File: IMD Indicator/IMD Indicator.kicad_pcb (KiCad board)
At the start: 2 copper layers, 55.5 x 38.8 mm, 11 parts, among them J1 172448-0004, J2 172448-0004, Q1 2N7002,215

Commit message: IMD Indicator
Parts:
- moved Reset1 3.26 mm to (83.8, 55.8)
- moved D2 2.06 mm to (97.2, 61.5)
- moved R20 2.06 mm to (97.2, 56.5)
- moved D7 1.00 mm to (76.8, 58.5)
- renumbered J2 to J1, J1 to J2
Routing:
- net Net-(D5-A): track 43.3 -> 39.8 mm
- net Net-(D2-K): track 24.2 -> 21.9 mm
- net /12V IGNITION: track 57.5 -> 55.7 mm
- net IMD KILL SIGNAL: track 55.5 -> 54.0 mm
- net Net-(D7-K): track 19.1 -> 17.9 mm
- net GND: track 36.6 -> 37.6 mm
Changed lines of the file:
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@@
 		(descr "172448-YY04")
 		(tags "Connector")
-		(property "Reference" "J1"
-			(at -2.2 -2 180)
+		(property "Reference" "J2"
+			(at -2.2 -2 0)
 			(layer "F.SilkS")
 			(effects
@@
 		(descr "172448-YY04")
 		(tags "Connector")
-		(property "Reference" "J2"
+		(property "Reference" "J1"
 			(at -2.1 -2.7 180)
 			(layer "F.SilkS")
@@
 	(footprint "Resistor_SMD:R_0603_1608Metric"
 		(layer "F.Cu")
-		(at 97.675 54.5 180)
+		(at 97.175 56.5 180)
 		(descr "Resistor SMD 0603 (1608 Metric), square (rectangular) end terminal, IPC-7351 nominal, (Body size source: IPC-SM-782 page 72, https://www.pcb-3d.com/wordpress/wp-content/uploads/ipc-sm-782a_amendment_1_and_2.pdf), generated with kicad-footprint-generator")
 		(tags "resistor")
@@
 	(footprint "SDM_MiscFootprint:SOT230P700X190-4N"
 		(layer "F.Cu")
-		(at 77.85 58.5)
+		(at 76.85 58.5)
 		(descr "SOT-223")
 		(tags "SCR")
@@
 	(footprint "SDM_MiscFootprint:SODFL1608X70N"
 		(layer "F.Cu")
-		(at 97.75 59.5)
+		(at 97.25 61.5)
 		(descr "SOD-523 CASE 502")
 		(tags "Diode")
@@
 	(footprint "Button_Switch_THT:SW_PUSH_6mm"
 		(layer "F.Cu")
-		(at 87 55.5)
+		(at 83.75 55.75)
 		(descr "Generic 6mm SW tactile push button")
 		(tags "tact sw push 6mm")
@@
 	)
 	(segment
-		(start 94 79.5)
-		(end 95 80.5)
-		(width 0.2)
+		(start 96.5 61.5)
+		(end 96.5 65.5)
+		(width 0.25)
 		(layer "F.Cu")
 		(net 1)
 	)
 	(segment
-		(start 96.5 62)
-		(end 96.5 65.5)
+		(start 94 79.5)
+		(end 95 80.5)
 		(width 0.2)
 		(layer "F.Cu")
@@
 	)
 	(segment
-		(start 97 59.5)
-		(end 97 61.5)
-		(width 0.2)
-		(layer "F.Cu")
-		(net 1)
-	)
-	(segment
-		(start 97 61.5)
-		(end 96.5 62)
-		(width 0.2)
-		(layer "F.Cu")
-		(net 1)
-	)
-	(segment
 		(start 77.7 70.5)
 		(end 77.3 70.9)
@@
 	)
 	(segment
-		(start 98.5 54.5)
-		(end 98.5 59.5)
+		(start 100 64)
+		(end 98 62)
 		(width 0.5)
 		(layer "F.Cu")
@@
 	)
 	(segment
-		(start 99 75)
-		(end 98 75)
+		(start 98 61.5)
+		(end 98 56.5)
 		(width 0.5)
 		(layer "F.Cu")
@@
 	)
 	(segment
-		(start 100 64)
-		(end 100 74)
+		(start 99 75)
+		(end 98 75)
 		(width 0.5)
 		(layer "F.Cu")
@@
 	)
 	(segment
-		(start 98.5 59.5)
-		(end 98.5 62.5)
+		(start 100 64)
+		(end 100 74)
 		(width 0.5)
 		(layer "F.Cu")
@@
 	)
 	(segment
-		(start 98.5 62.5)
-		(end 100 64)
+		(start 98 62)
+		(end 98 61.5)
 		(width 0.5)
 		(layer "F.Cu")
@@
 	)
 	(segment
-		(start 74.7 60.8)
-		(end 74.7 62.8)
-		(width 0.2)
+		(start 71.5 66)
+		(end 73.7 63.8)
+		(width 0.25)
+		(layer "F.Cu")
+		(net 4)
+	)
+	(segment
+		(start 73.7 63.8)
+		(end 73.7 60.8)
+		(width 0.25)
 		(layer "F.Cu")
 		(net 4)
@@
 	)
 	(segment
-		(start 74.7 62.8)
-		(end 71.5 66)
-		(width 0.2)
-		(layer "F.Cu")
-		(net 4)
-	)
-	(segment
 		(start 74.2 79.8)
 		(end 74 80)
@@
 	)
 	(segment
-		(start 96.85 58.518)
-		(end 91.368 64)
-		(width 0.2)
-		(layer "F.Cu")
-		(net 5)
-	)
-	(segment
-		(start 91.368 64)
-		(end 91.368 65.5)
-		(width 0.2)
-		(layer "F.Cu")
-		(net 5)
-	)
-	(segment
-		(start 96.85 54.5)
-		(end 96.85 58.518)
-		(width 0.2)
-		(layer "F.Cu")
-		(net 5)
-	)
-	(segment
-		(start 90.868 66)
-		(end 88.5 66)
-		(width 0.2)
+		(start 96.35 58.15)
+		(end 96.35 56.5)
+		(width 0.25)
 		(layer "F.Cu")
 		(net 5)
 	)
 	(segment
-		(start 91.368 65.5)
-		(end 90.868 66)
-		(width 0.2)
+		(start 88.5 66)
+		(end 96.35 58.15)
+		(width 0.25)
 		(layer "F.Cu")
 		(net 5)
@@
 	)
 	(segment
-		(start 85.96 84.5)
-		(end 85.96 84.96)
-		(width 0.2)
-		(layer "F.Cu")
-		(net 6)
-	)
-	(segment
 		(start 92.5 75)
 		(end 92.5 76.96)
@@
 	)
 	(segment
-		(start 81 64.5)
-		(end 74.854 70.646)
+		(start 80 58.5)
+		(end 73.7 58.5)
 		(width 0.25)
 		(layer "F.Cu")
@@
 	)
 	(segment
-		(start 85.96 84.96)
-		(end 86 85)
-		(width 0.2)
+		(start 74.854 70.646)
+		(end 80 65.5)
+		(width 0.25)
 		(layer "F.Cu")
 		(net 6)
 	)
 	(segment
-		(start 81 58.5)
-		(end 74.7 58.5)
+		(start 74.854 70.646)
+		(end 74.854 80.536)
 		(width 0.25)
 		(layer "F.Cu")
@@
 	)
 	(segment
-		(start 81 58.5)
-		(end 81 64.5)
+		(start 74.854 80.536)
+		(end 77.818 83.5)
 		(width 0.25)
 		(layer "F.Cu")
@@
 	)
 	(segment
-		(start 74.854 70.646)
-		(end 74.854 80.536)
+		(start 80 65.5)
+		(end 80 58.5)
 		(width 0.25)
 		(layer "F.Cu")
@@
 	)
 	(segment
-		(start 85.96 85.04)
-		(end 85.96 84.5)
+		(start 73.7 56.2)
+		(end 83.3 56.2)
 		(width 0.25)
 		(layer "F.Cu")
-		(net 6)
+		(net 7)
 	)
 	(segment
-		(start 74.854 80.536)
-		(end 77.818 83.5)
+		(start 83.75 55.75)
+		(end 83.25 55.75)
 		(width 0.25)
 		(layer "F.Cu")
-		(net 6)
+		(net 7)
 	)
 	(segment
-		(start 93.5 55.5)
-		(end 87 55.5)
-		(width 0.2)
+		(start 83.3 56.2)
+		(end 83.75 55.75)
+		(width 0.25)
 		(layer "F.Cu")
 		(net 7)
 	)
 	(segment
-		(start 74.7 56.2)
-		(end 86.3 56.2)
+		(start 90.25 55.75)
+		(end 83.75 55.75)
 		(width 0.25)
 		(layer "F.Cu")
@@
 	)
 	(segment
-		(start 86.3 56.2)
-		(end 87 55.5)
+		(start 84.3 56.2)
+		(end 84.75 55.75)
 		(width 0.25)
 		(layer "F.Cu")
@@
 	)
 	(segment
-		(start 85.65 69.35)
+		(start 84.55 66.55)
 		(end 85.65 67.65)
 		(width 0.2)
@@
 	)
 	(segment
-		(start 84.5 70.5)
-		(end 85.65 69.35)
+		(start 84.55 65.05)
+		(end 84.55 66.55)
 		(width 0.2)
 		(layer "F.Cu")
@@
 	)
 	(segment
-		(start 84.5 65)
-		(end 84.55 65.05)
+		(start 85.65 69.35)
+		(end 85.65 67.65)
 		(width 0.2)
 		(layer "F.Cu")
@@
 	)
 	(segment
-		(start 85.65 67.65)
-		(end 84.5 66.5)
+		(start 84.5 70.5)
+		(end 85.65 69.35)
 		(width 0.2)
 		(layer "F.Cu")
@@
 	)
 	(segment
-		(start 84.5 66.5)
-		(end 84.5 65)
-		(width 0.2)
-		(layer "F.Cu")
-		(net 8)
-	)
-	(segment
 		(start 92.075 82)
 		(end 90.575 83.5)
@@
 	)
 	(segment
-		(start 87 60)
-		(end 87.626 60.626)
-		(width 0.2)
+		(start 87.5 65.75)
+		(end 86.3 66.95)
+		(width 0.25)
 		(layer "F.Cu")
 		(net 10)
 	)
 	(segment
-		(start 87.626 60.626)
-		(end 87.626 65.624)
+		(start 90.25 60.25)
+		(end 83.75 60.25)
 		(width 0.5)
 		(layer "F.Cu")
@@
 	)
 	(segment
-		(start 83.3 74.6)
-		(end 82.8 75.1)
-		(width 0.2)
+		(start 87.5 64)
+		(end 87.5 65.75)
+		(width 0.25)
 		(layer "F.Cu")
 		(net 10)
 	)
 	(segment
-		(start 87.626 65.624)
-		(end 86.3 66.95)
-		(width 0.5)
+		(start 83.3 74.6)
+		(end 82.8 75.1)
+		(width 0.2)
 		(layer "F.Cu")
 		(net 10)
@@
 	)
 	(segment
-		(start 85.5 71.5)
-		(end 85.5 72.4)
-		(width 0.5)
-		(layer "B.Cu")
+		(start 83.75 60.25)
+		(end 87.5 64)
+		(width 0.25)
+		(layer "F.Cu")
 		(net 10)
 	)
 	(segment
-		(start 87 60)
-		(end 93.5 60)
+		(start 85.5 71.5)
+		(end 85.5 72.4)
 		(width 0.5)
 		(layer "B.Cu")

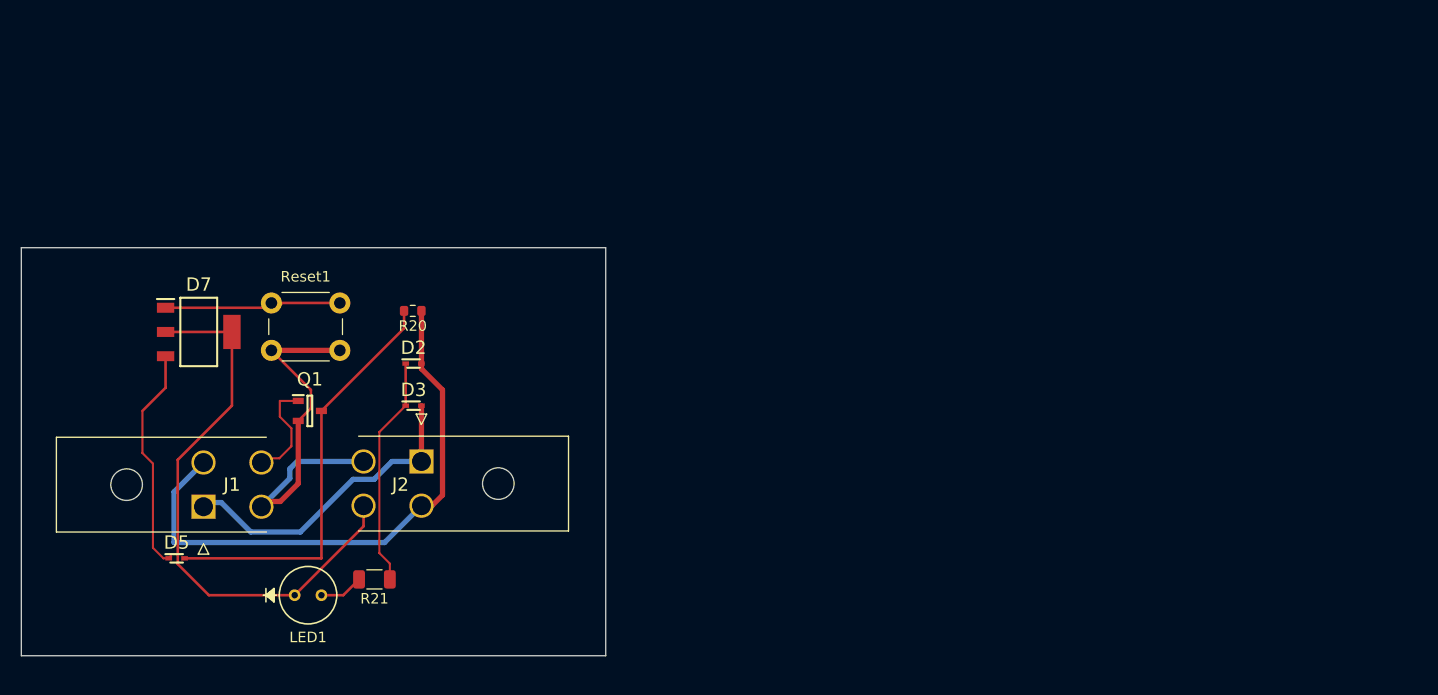
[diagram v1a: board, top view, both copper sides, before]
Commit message: fixed reset button and connect logic signal to SCR gate
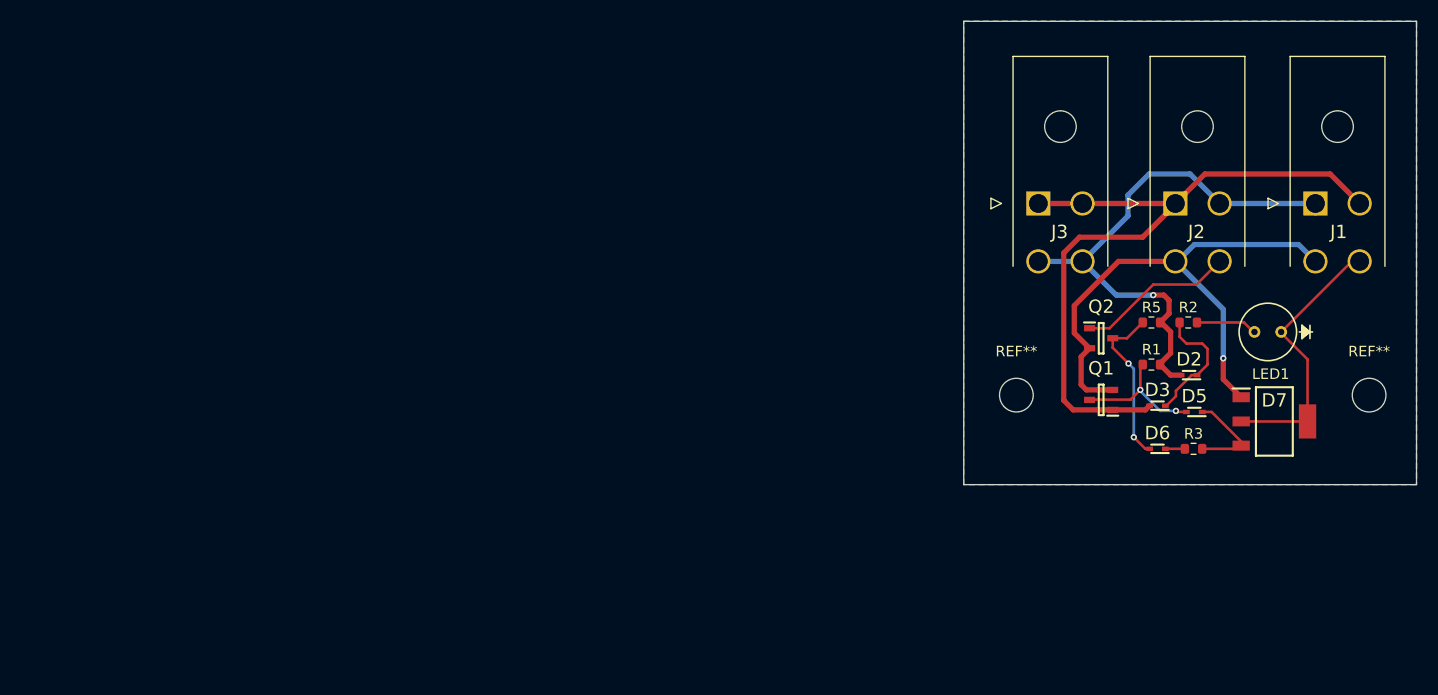
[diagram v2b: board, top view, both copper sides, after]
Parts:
- removed R20: 10k, Resistor_SMD:R_0603_1608Metric
- removed R21: 510, Resistor_SMD:R_1206_3216Metric
- removed Reset1: SW_Push_Open, Button_Switch_THT:SW_PUSH_6mm
- added D6: BAT54XV2T1G, SDM_MiscFootprint:SODFL1608X70N, F.Cu at (167.9, 69.6)
- added J3: 172448-0004, IMDFootprintLibrary:172448-YY04, F.Cu at (156.6, 46.3)
- added Q2: 2N7002,215, SDM_MiscFootprint:SOT95P230X110-3N, F.Cu at (162.6, 59.1)
- added R1: 10k, Resistor_SMD:R_0603_1608Metric, F.Cu at (167.3, 61.6)
- added R2: 510, Resistor_SMD:R_0603_1608Metric, F.Cu at (170.8, 57.6)
- added R3: 1k, Resistor_SMD:R_0603_1608Metric, F.Cu at (171.3, 69.6)
- added R5: 10k, Resistor_SMD:R_0603_1608Metric, F.Cu at (167.3, 57.6)
- added REF**: MountingHole_3.2mm_M3, MountingHole:MountingHole_3.2mm_M3, F.Cu at (154.5, 64.5)
- added REF**: MountingHole_3.2mm_M3, MountingHole:MountingHole_3.2mm_M3, F.Cu at (188.0, 64.5)
- moved J1 109.5 mm to (182.9, 46.3), turned to 180 degrees
- moved D7 102.5 mm to (179.0, 67.0)
- moved D5 97.6 mm to (171.4, 66.1), turned to 180 degrees
- moved LED1 97.0 mm to (179.7, 58.5), turned to 180 degrees
- moved J2 75.7 mm to (169.6, 46.3), turned to 180 degrees
- moved Q1 75.2 mm to (162.6, 65.0), turned to 180 degrees
- moved D2 73.7 mm to (170.9, 62.6), turned to 180 degrees
- moved D3 70.7 mm to (167.9, 65.5), turned to 180 degrees
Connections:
- D7 pad 1: Net-(D7-K) -> GND
- J1 pad 1: /12V MASTER -> /12V IGNITION
- J1 pad 2: /12V IGNITION -> /12V MASTER
- J1 pad 4: /IMD_Logic_Signal -> IMD KILL SIGNAL
- J2 pad 4: IMD KILL SIGNAL -> /IMD_LOGIC_SIGNAL
- Q1 pad 1: /IMD_Logic_Signal -> /12V MASTER
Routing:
- net /12V MASTER: track 30.1 -> 68.7 mm
- net IMD KILL SIGNAL: track 54.0 -> 25.6 mm
- net Net-(D5-A): track 39.8 -> 13.4 mm, vias 0 -> 2
- net Net-(D7-K): track 17.9 -> 0.00 mm
- net GND: track 37.6 -> 53.4 mm, vias 0 -> 1
- net Net-(D6-A): track 0.00 -> 15.7 mm, vias 0 -> 2
- net /IMD_LOGIC_SIGNAL: track 0.00 -> 15.0 mm
- net /SCR Gate: track 21.7 -> 8.85 mm
- net Net-(D2-K): track 21.9 -> 11.9 mm
- net /IMD_Logic_Signal: track 10.00 -> 0.00 mm
- net /12V IGNITION: track 55.7 -> 52.6 mm, vias 0 -> 1
- net Net-(D6-K): track 0.00 -> 1.85 mm
- net Net-(LED1-Pad2): track 4.20 -> 5.87 mm
- added copper zone on B.Cu, net GND
- added copper zone on F.Cu, net GND
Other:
- board size 55.5 x 38.8 mm -> 43 x 44 mm

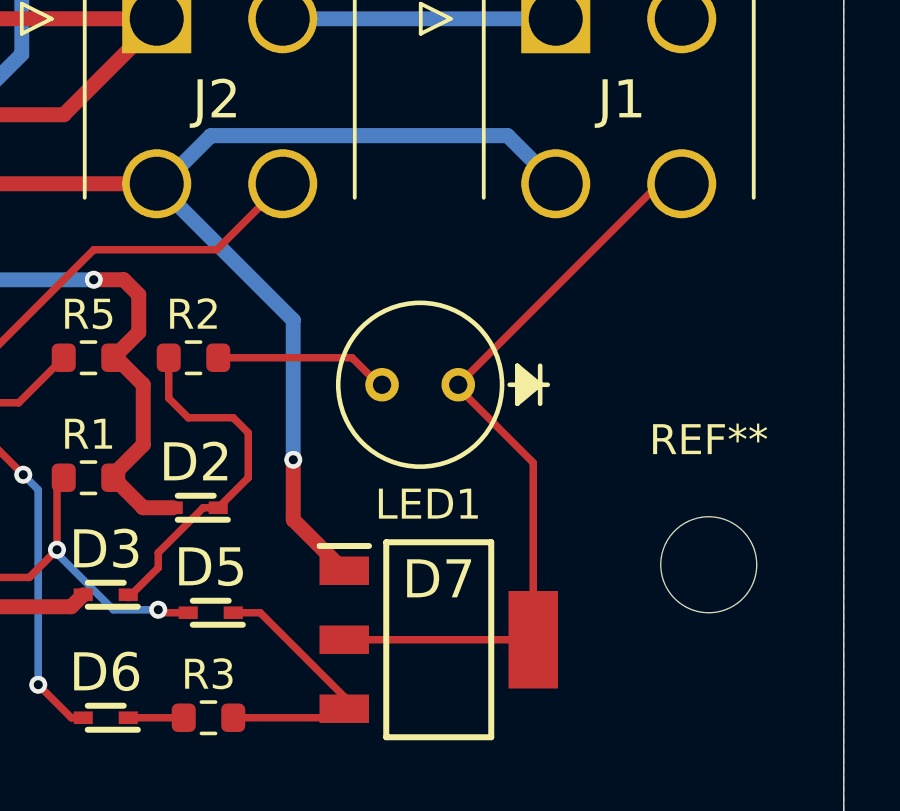
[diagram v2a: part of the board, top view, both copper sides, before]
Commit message: changed LED (symbol, footprint)
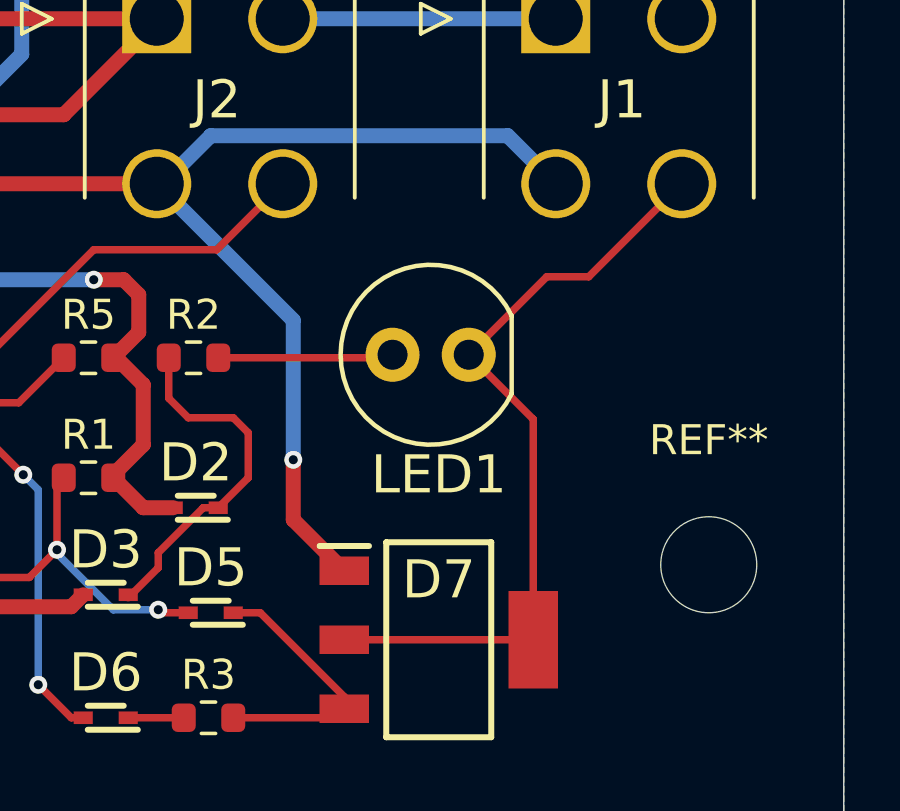
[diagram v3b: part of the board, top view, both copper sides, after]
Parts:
- LED1: value HLMP-EG08-WZ000 -> HLMP-EG30-NR000; footprint IMDFootprintLibrary:LED_-WZ000 -> IMDFootprintLibrary:LED_5MM
- moved LED1 1.36 mm to (178.7, 57.5)
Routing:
- net IMD KILL SIGNAL: track 25.6 -> 26.5 mm

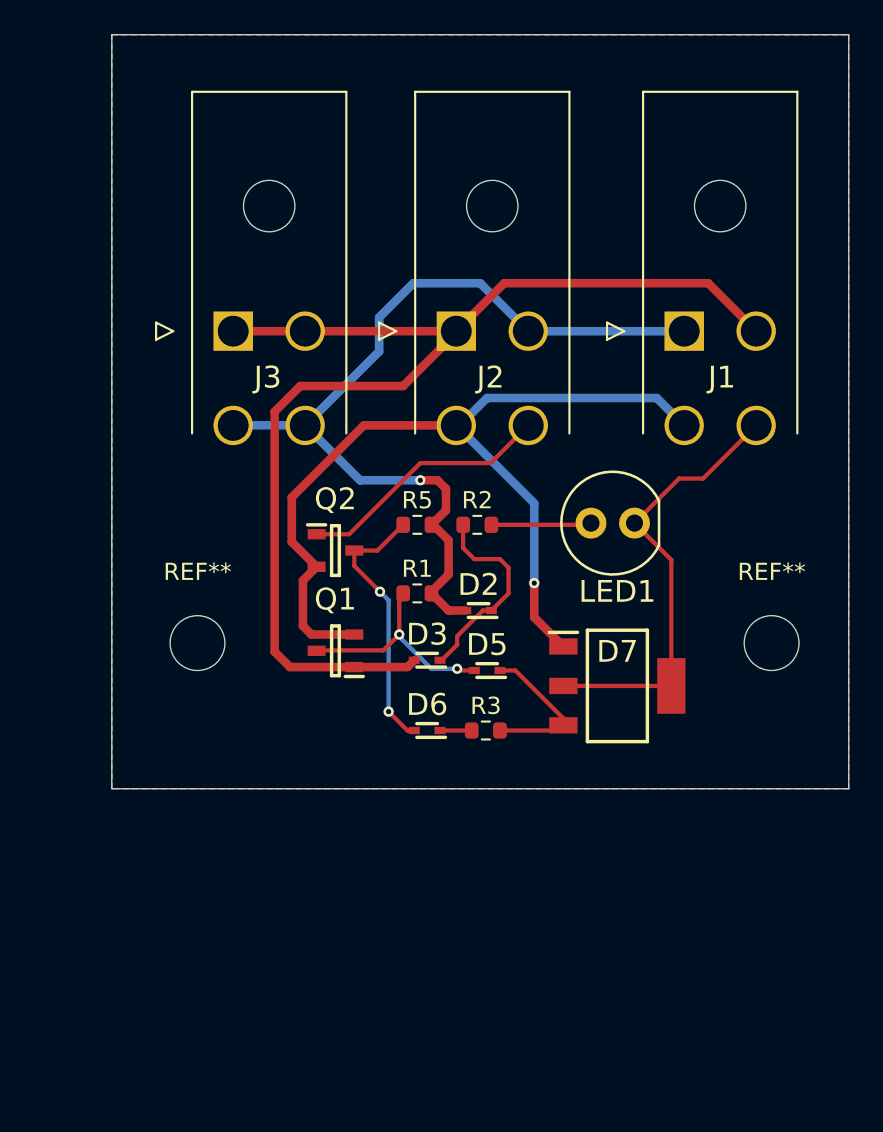
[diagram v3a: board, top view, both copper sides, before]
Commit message: removed unnecessary connectors from sch & layout, added pulldown resistor
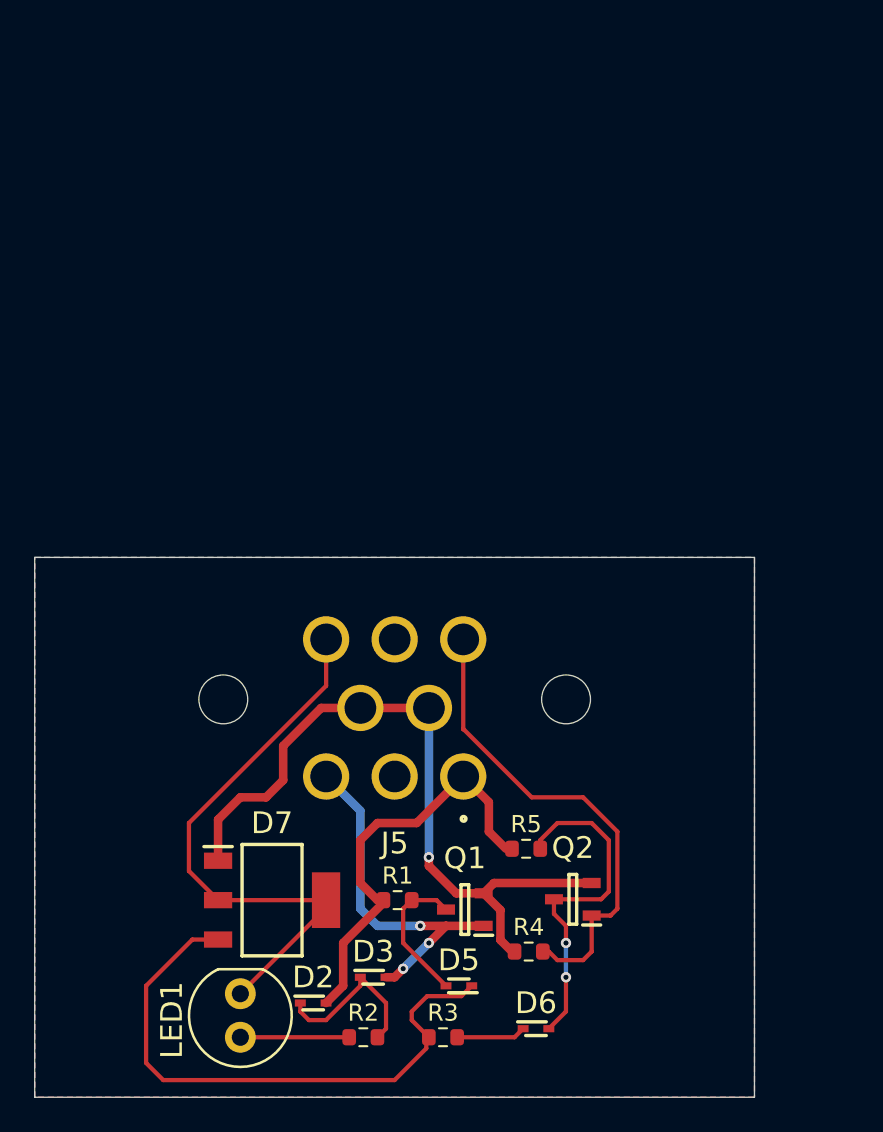
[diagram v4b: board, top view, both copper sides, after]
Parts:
- removed J1, J2, J3: 172448-0004, IMDFootprintLibrary:172448-YY04
- removed REF** (x2): MountingHole_3.2mm_M3, MountingHole:MountingHole_3.2mm_M3
- added J5: 776280-1, SDM_MiscFootprint:776280-1, F.Cu at (166.0, 56.5)
- added R4: 2.2k, Resistor_SMD:R_0603_1608Metric, F.Cu at (173.8, 82.5)
- moved LED1 36.0 mm to (157.0, 86.2), turned to -90 degrees
- moved R2 30.6 mm to (164.2, 87.5), turned to 180 degrees
- moved D2 24.9 mm to (161.2, 85.5), turned to 0 degrees
- moved Q2 24.6 mm to (176.4, 79.5), turned to 180 degrees
- moved D7 23.7 mm to (158.8, 79.5)
- moved R5 19.9 mm to (173.7, 76.5), turned to 0 degrees
- moved D3 18.8 mm to (164.8, 84.0), turned to 0 degrees
- moved D6 18.5 mm to (174.2, 87.0), turned to 0 degrees
- moved D5 18.5 mm to (169.8, 84.5)
- moved R3 18.1 mm to (168.8, 87.5), turned to 0 degrees
- moved R1 17.9 mm to (166.2, 79.5), turned to 0 degrees
- moved Q1 16.9 mm to (170.1, 80.0)
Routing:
- net /12V MASTER: track 68.7 -> 20.9 mm, vias 0 -> 3
- net /12V IGNITION: track 52.6 -> 24.4 mm, vias 1 -> 0
- net /SCR Gate: track 8.85 -> 34.0 mm
- net /IMD_LOGIC_SIGNAL: track 15.0 -> 28.4 mm
- net GND: track 53.4 -> 42.3 mm
- net IMD KILL SIGNAL: track 26.5 -> 33.1 mm
- net Net-(D5-A): track 13.4 -> 8.47 mm, vias 2 -> 0
- net Net-(D6-A): track 15.7 -> 20.0 mm
- net Net-(D6-K): track 1.85 -> 4.21 mm
- net Net-(D2-K): track 11.9 -> 9.86 mm
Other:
- board size 43 x 44 mm -> 42 x 31.5 mm
